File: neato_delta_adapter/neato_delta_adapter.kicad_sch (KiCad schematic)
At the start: 11 parts, among them J1 JST PH2.0 B4B Vert, J2 JST PH2.0 B2B Vert, J3 JST PH B4B Vert, J4 DNP JST PH2.0 B5B Vert, Q1 AS2302, U1 DNP LM2596

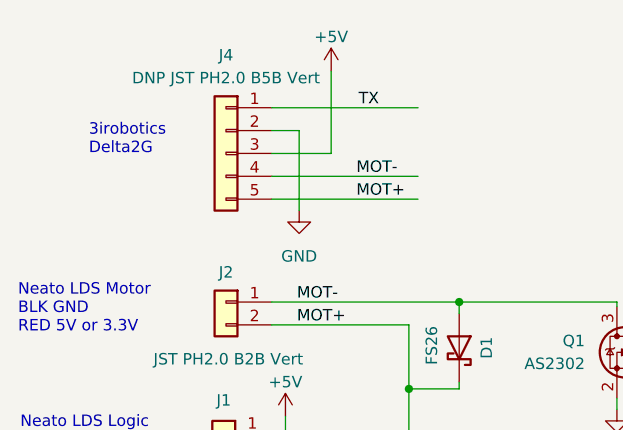
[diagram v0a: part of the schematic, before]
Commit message: Level shifter for Delta
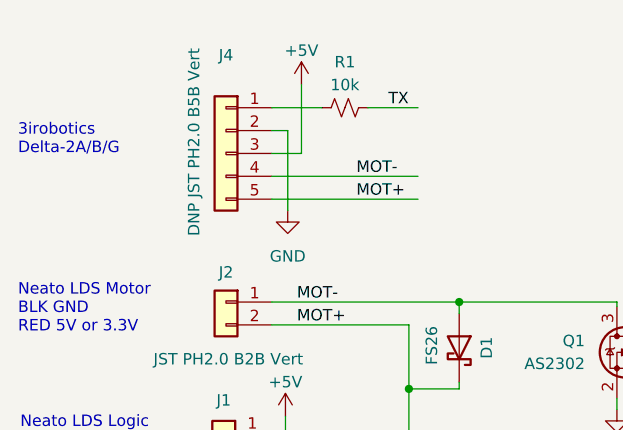
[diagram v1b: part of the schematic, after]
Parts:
- added R1: 10k, Resistor_SMD:R_0603_1608Metric, symbol Device:R_Small_US
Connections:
- net TX: now also R1.1; no longer J4.1 (Pin_1)
- new net: J4.1 (Pin_1), R1.2
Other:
- note added: "3irobotics Delta-2A/B/G"
- note removed: "3irobotics Delta2G"

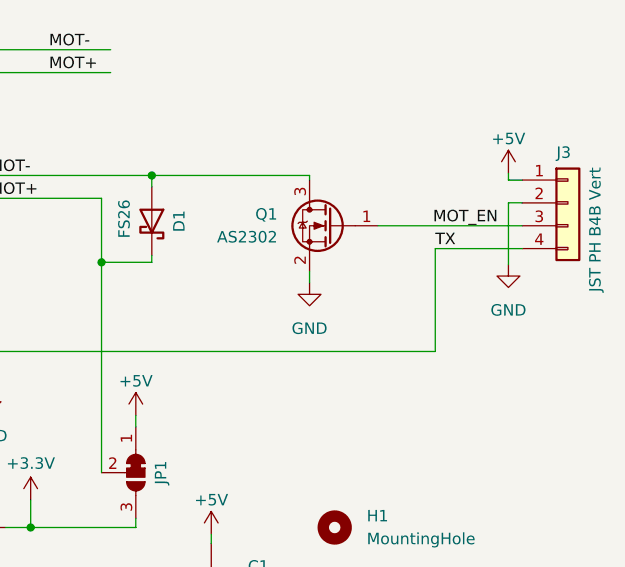
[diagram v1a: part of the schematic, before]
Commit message: Delta motor enable pulldown
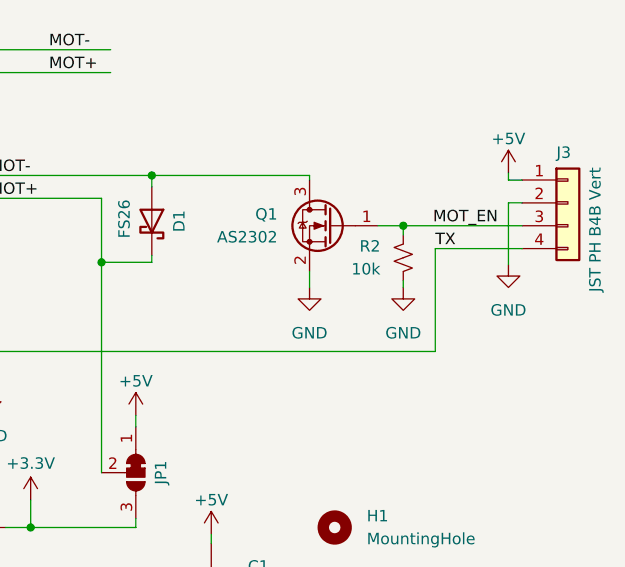
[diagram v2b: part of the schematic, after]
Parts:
- added R2: 10k, Resistor_SMD:R_0603_1608Metric, symbol Device:R_Small_US
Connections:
- net GND: now also R2.1
- net MOT_EN: now also R2.2
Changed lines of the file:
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@@
   (junction (at 92.202 43.942) (diameter 0) (color 0 0 0 0)
+  )
+  (junction (at 120.142 49.53) (diameter 0) (color 0 0 0 0)
   )
   (junction (at 86.614 53.594) (diameter 0) (color 0 0 0 0)
@@
     (stroke (width 0) (type default))
   )
+  (wire (pts (xy 120.142 55.626) (xy 120.142 56.388))
+    (stroke (width 0) (type default))
+  )
   (wire (pts (xy 75.946 83.058) (xy 78.74 83.058))
     (stroke (width 0) (type default))
@@
     (stroke (width 0) (type default))
   )
-  (wire (pts (xy 109.728 54.61) (xy 109.728 55.88))
+  (wire (pts (xy 109.728 54.61) (xy 109.728 56.388))
     (stroke (width 0) (type default))
   )
@@
     (stroke (width 0) (type default))
   )
-  (wire (pts (xy 117.348 49.53) (xy 133.35 49.53))
+  (wire (pts (xy 117.348 49.53) (xy 120.142 49.53))
     (stroke (width 0) (type default))
   )
@@
   )
   (wire (pts (xy 78.74 83.058) (xy 90.424 83.058))
+    (stroke (width 0) (type default))
+  )
+  (wire (pts (xy 120.142 49.53) (xy 120.142 50.546))
+    (stroke (width 0) (type default))
+  )
+  (wire (pts (xy 120.142 49.53) (xy 133.35 49.53))
     (stroke (width 0) (type default))
   )
@@
     )
   )
-  (symbol (lib_id "power:GND") (at 109.728 55.88 0) (unit 1)
-    (in_bom yes) (on_board yes) (dnp no) (fields_autoplaced)
-    (property "Reference" "#PWR02" (at 109.728 62.23 0)
-      (effects (font (size 1.27 1.27)) hide)
-    )
-    (property "Value" "GND" (at 109.728 60.96 0)
-      (effects (font (size 1.27 1.27)))
-    )
-    (property "Footprint" "" (at 109.728 55.88 0)
-      (effects (font (size 1.27 1.27)) hide)
-    )
-    (property "Datasheet" "" (at 109.728 55.88 0)
+  (symbol (lib_id "power:GND") (at 109.728 56.388 0) (unit 1)
+    (in_bom yes) (on_board yes) (dnp no) (fields_autoplaced)
+    (property "Reference" "#PWR02" (at 109.728 62.738 0)
+      (effects (font (size 1.27 1.27)) hide)
+    )
+    (property "Value" "GND" (at 109.728 61.468 0)
+      (effects (font (size 1.27 1.27)))
+    )
+    (property "Footprint" "" (at 109.728 56.388 0)
+      (effects (font (size 1.27 1.27)) hide)
+    )
+    (property "Datasheet" "" (at 109.728 56.388 0)
       (effects (font (size 1.27 1.27)) hide)
     )
@@
         (path "/c13da21a-388e-44a0-831a-aa3d56cf7c53"
           (reference "#PWR010") (unit 1)
+        )
+      )
+    )
+  )
+  (symbol (lib_id "power:GND") (at 120.142 56.388 0) (unit 1)
+    (in_bom yes) (on_board yes) (dnp no) (fields_autoplaced)
+    (property "Reference" "#PWR015" (at 120.142 62.738 0)
+      (effects (font (size 1.27 1.27)) hide)
+    )
+    (property "Value" "GND" (at 120.142 61.468 0)
+      (effects (font (size 1.27 1.27)))
+    )
+    (property "Footprint" "" (at 120.142 56.388 0)
+      (effects (font (size 1.27 1.27)) hide)
+    )
+    (property "Datasheet" "" (at 120.142 56.388 0)
+      (effects (font (size 1.27 1.27)) hide)
+    )
+    (pin "1")
+    (instances
+      (project "neato_delta_adapter"
+        (path "/c13da21a-388e-44a0-831a-aa3d56cf7c53"
+          (reference "#PWR015") (unit 1)
+        )
+      )
+      (project "esp32_breakout"
+        (path "/e24ae185-8f18-408c-aee8-f727519bade3"
+          (reference "#PWR011") (unit 1)
         )
       )
@@
         )
       )
+    )
+  )
+  (symbol (lib_id "Device:R_Small_US") (at 120.142 53.086 0) (mirror x) (unit 1)
+    (in_bom yes) (on_board yes) (dnp no)
+    (property "Reference" "R2" (at 117.602 51.816 0)
+      (effects (font (size 1.27 1.27)) (justify right))
+    )
+    (property "Value" "10k" (at 117.602 54.356 0)
+      (effects (font (size 1.27 1.27)) (justify right))
+    )
+    (property "Footprint" "Resistor_SMD:R_0603_1608Metric" (at 120.142 53.086 0)
+      (effects (font (size 1.27 1.27)) hide)
+    )
+    (property "Datasheet" "~" (at 120.142 53.086 0)
+      (effects (font (size 1.27 1.27)) hide)
+    )
+    (pin "1")
+    (pin "2")
+    (instances
+      (project "neato_delta_adapter"
+        (path "/c13da21a-388e-44a0-831a-aa3d56cf7c53"
+          (reference "R2") (unit 1)
+        )
+      )
+      (project "esp32_breakout"
+        (path "/e24ae185-8f18-408c-aee8-f727519bade3"
+          (reference "R3") (unit 1)
+        )
+      )

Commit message: Schematic notes
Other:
- note added: "3irobotics Delta-2A/B/G TX GND 5V MOT- MOT+"
- note added: "To ESP32 Breakout Board LDS connector 5V GND MOT_EN TX"
- note removed: "3irobotics Delta-2A/B/G"
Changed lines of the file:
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@@
+    (effects (font (size 1.27 1.27)) (justify left bottom))
+  )
+  (text "To ESP32 Breakout\nBoard LDS connector\n\n5V\nGND\nMOT_EN\nTX"
+    (at 145.796 51.816 0)
     (effects (font (size 1.27 1.27)) (justify left bottom))
   )
@@
     (effects (font (size 1.27 1.27)) (justify left bottom))
   )
-  (text "3irobotics\nDelta-2A/B/G" (at 43.18 27.686 0)
+  (text "3irobotics\nDelta-2A/B/G\n\nTX\nGND\n5V\nMOT-\nMOT+" (at 43.18 32.004 0)
     (effects (font (size 1.27 1.27)) (justify left bottom))
   )
